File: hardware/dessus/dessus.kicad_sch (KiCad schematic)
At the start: 0 parts

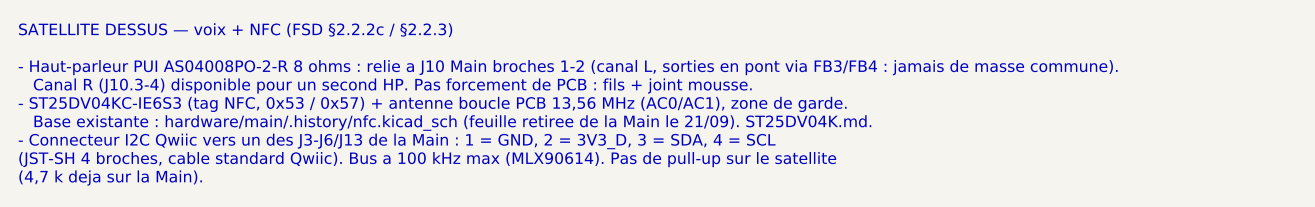
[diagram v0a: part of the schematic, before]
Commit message: hardware+docs: CAP1298 retenu pour le tactile de Cote 2, BOM de reference corrigee (H8)
- Cote 2 : CAP1298-1-SL-TR (C2652072, 8 touches, 0x28 fixe) remplace le MTCH2120
  (aucun stock) ; proximite de Cote 3 en suspens (pas de second CAP12xx).
- BOM : U11 = LSM6DSOXTR, doublon U21 retire, filtre DAC 470 ohm + 2,2 nF C0G,
  TMAG5273A1 (C3716049), U10 SOT-23-6, ecran bouche a choisir, LCSC de D1/Q1/Q2
  dans la bonne colonne, ST25DV et haut-parleur ajoutes.
- docs/pcb/02-bom-lcsc.csv (perimee) supprimee : une seule BOM.
- FSD, RESTE-A-FAIRE, syntheses et cartouches satellites alignes.
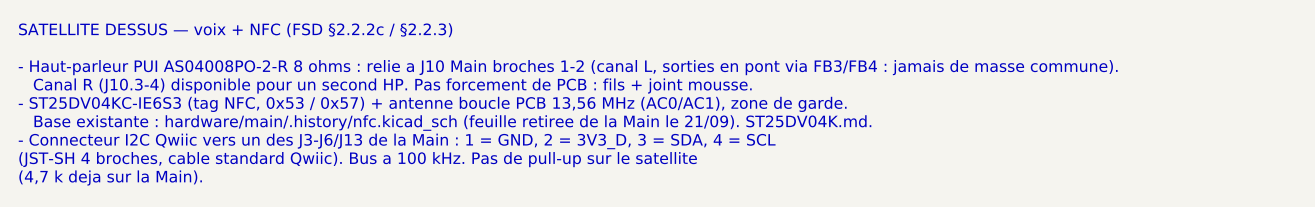
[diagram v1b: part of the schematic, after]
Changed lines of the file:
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@@
 	(generator_version "10.0")
 	(paper "A4")
-	(text "SATELLITE DESSUS — voix + NFC (FSD §2.2.2c / §2.2.3)\n\n- Haut-parleur PUI AS04008PO-2-R 8 ohms : relie a J10 Main broches 1-2 (canal L, sorties en pont via FB3/FB4 : jamais de masse commune).\n   Canal R (J10.3-4) disponible pour un second HP. Pas forcement de PCB : fils + joint mousse.\n- ST25DV04KC-IE6S3 (tag NFC, 0x53 / 0x57) + antenne boucle PCB 13,56 MHz (AC0/AC1), zone de garde.\n   Base existante : hardware/main/.history/nfc.kicad_sch (feuille retiree de la Main le 21/09). ST25DV04K.md.\n- Connecteur I2C Qwiic vers un des J3-J6/J13 de la Main : 1 = GND, 2 = 3V3_D, 3 = SDA, 4 = SCL\n(JST-SH 4 broches, cable standard Qwiic). Bus a 100 kHz max (MLX90614). Pas de pull-up sur le satellite\n(4,7 k deja sur la Main)."
+	(text "SATELLITE DESSUS — voix + NFC (FSD §2.2.2c / §2.2.3)\n\n- Haut-parleur PUI AS04008PO-2-R 8 ohms : relie a J10 Main broches 1-2 (canal L, sorties en pont via FB3/FB4 : jamais de masse commune).\n   Canal R (J10.3-4) disponible pour un second HP. Pas forcement de PCB : fils + joint mousse.\n- ST25DV04KC-IE6S3 (tag NFC, 0x53 / 0x57) + antenne boucle PCB 13,56 MHz (AC0/AC1), zone de garde.\n   Base existante : hardware/main/.history/nfc.kicad_sch (feuille retiree de la Main le 21/09). ST25DV04K.md.\n- Connecteur I2C Qwiic vers un des J3-J6/J13 de la Main : 1 = GND, 2 = 3V3_D, 3 = SDA, 4 = SCL\n(JST-SH 4 broches, cable standard Qwiic). Bus a 100 kHz. Pas de pull-up sur le satellite\n(4,7 k deja sur la Main)."
 		(exclude_from_sim no)
 		(at 20.32 142.24 0)

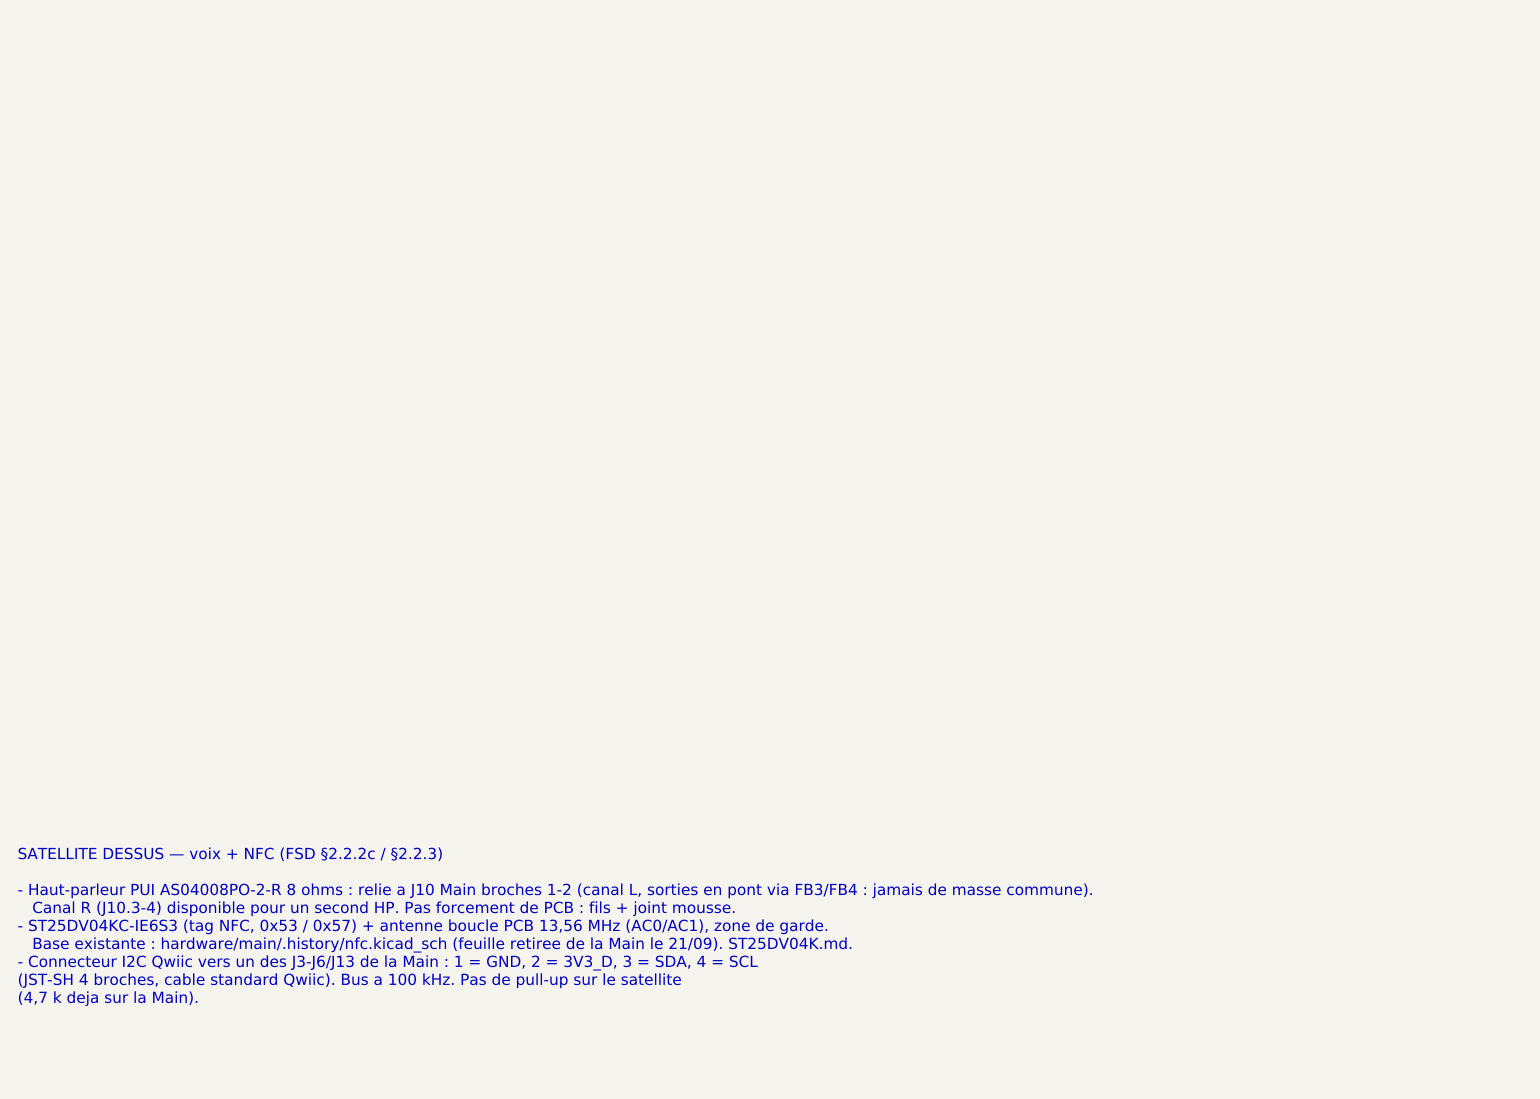
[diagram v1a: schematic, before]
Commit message: hardware: schemas des satellites Dessus, Devant, Cote 1 et Cote 3
- Dessus : ST25DV04KC (10 nF + 100 nF), antenne boucle ANT1 (~4,8 uH, empreinte a creer), accord C3 DNP, Qwiic
- Devant : BMP280 (CSB sur VDDIO, SDO GND), VEML7700, liaisons J7/J7b/J9, embases yeux/bouche provisoires, halo 8 WS2812B
- Cote 1 : ADS7830 ratiometrique, 4 faders PTA6043, 4 pots PDB181, liaison J8, toggles/boutons en facade sur JST-PH
- Cote 3 : TMAG5273A1 (INT et TEST a GND), 100 nF, Qwiic
- BOM : lignes satellites prefixees par face, recoupees avec les schemas
- Brochages corriges dans les syntheses : ST25DV (1 V_EH, 2 AC0) et VEML7700 (2 VDD, 4 SDA)
- Questions ouvertes : docs/audits/2026-09-27-questions-satellites.md
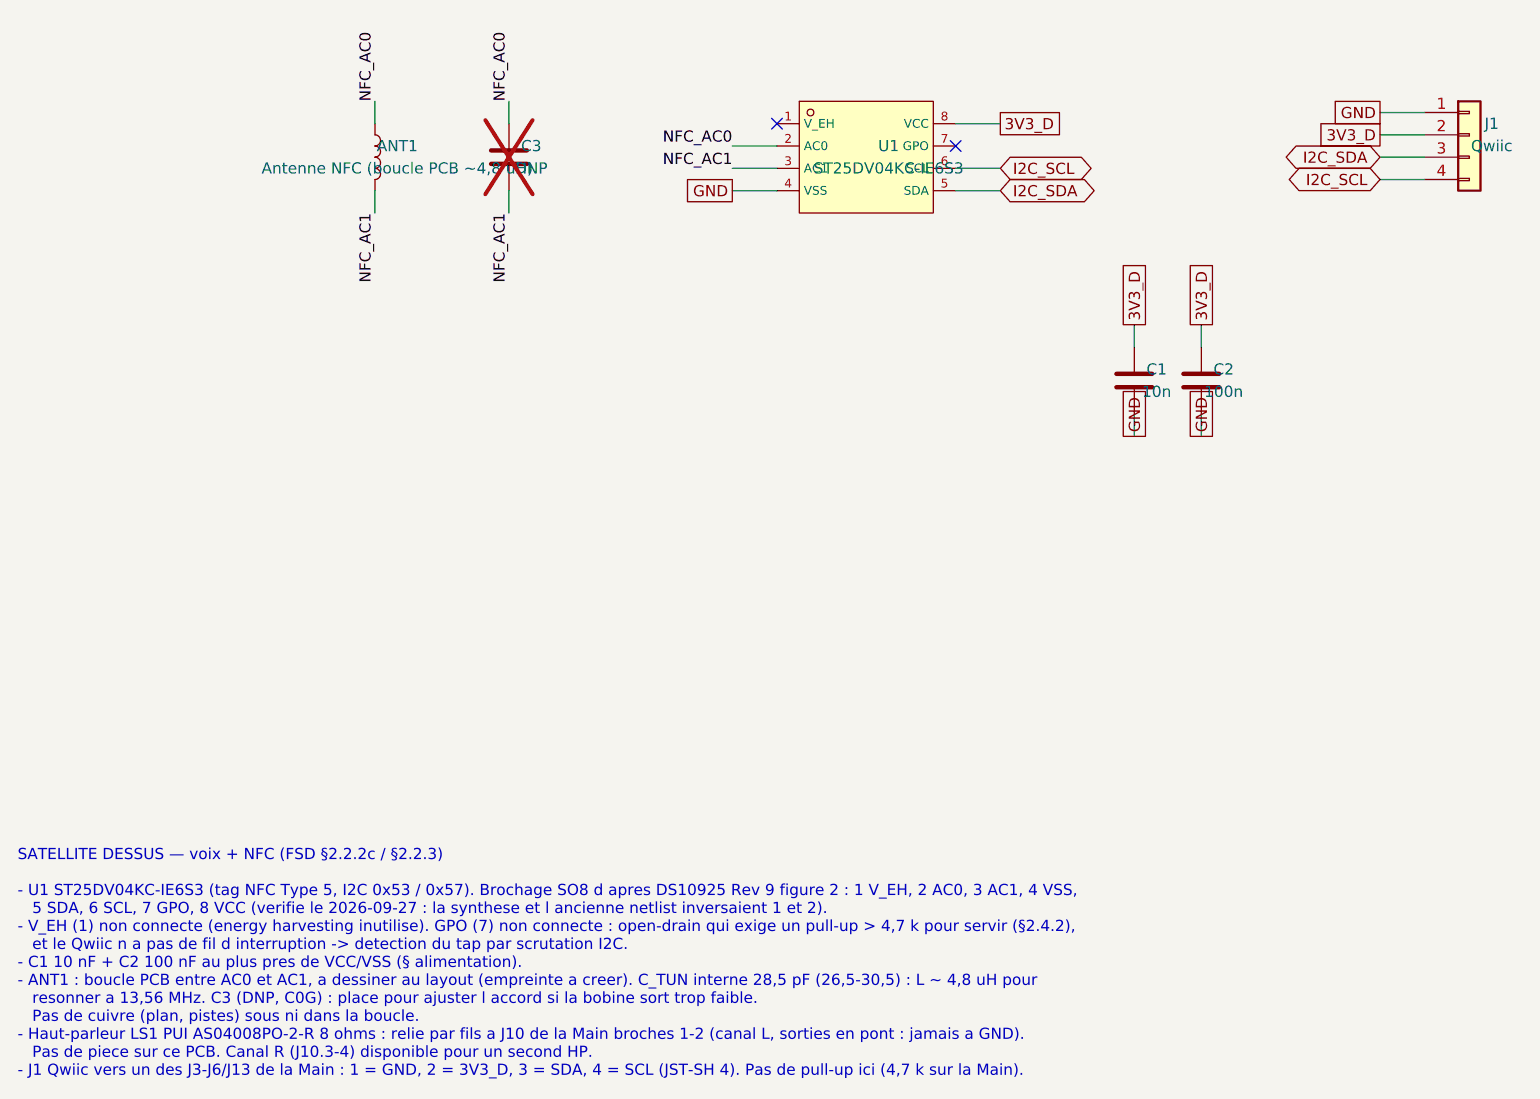
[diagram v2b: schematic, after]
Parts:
- added ANT1: Antenne NFC (boucle PCB ~4,8 uH), symbol Device:L
- added C1: 10n, Capacitor_SMD:C_0402_1005Metric, symbol Device:C
- added C2: 100n, Capacitor_SMD:C_0402_1005Metric, symbol Device:C
- added C3: DNP, Capacitor_SMD:C_0402_1005Metric, symbol Device:C
- added J1: Qwiic, Connector_JST:JST_SH_BM04B-SRSS-TB_1x04-1MP_P1.00mm_Vertical, symbol Connector_Generic:Conn_01x04
- added U1: ST25DV04KC-IE6S3, lcsc_footprints:C3304276_SO-8_L4_9-W3_9-P1_27-LS5_9-BL, symbol lcsc_imported:ST25DV04KC-IE6S3
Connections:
- new net 3V3_D: C1.1, C2.1, J1.2 (Pin_2), U1.8 (VCC)
- new net GND: C1.2, C2.2, J1.1 (Pin_1), U1.4 (VSS)
- new net I2C_SCL: J1.4 (Pin_4), U1.6 (SCL)
- new net I2C_SDA: J1.3 (Pin_3), U1.5 (SDA)
- new net NFC_AC0: ANT1.1, C3.1, U1.2 (AC0)
- new net NFC_AC1: ANT1.2, C3.2, U1.3 (AC1)
- no-connect marks 0 -> 2
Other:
- note added: "SATELLITE DESSUS — voix + NFC (FSD §2.2.2c / §2.2.3) - U1 ST25DV04KC-IE6S3 (tag NFC Type 5, I2C 0x53 / 0x57). Brochage SO8 d apres DS10925 Rev 9 figure 2 : 1 V_EH, 2 AC0, 3 AC1, 4 VSS, 5 SDA, 6 SCL, 7 GPO, 8 VCC (verifie le 2026-09-27 : la synthese et l ancienne netlist inversaient 1 et 2). - V_EH (1) non connecte (energy harvesting inutilise). GPO (7) non connecte : open-drain qui exige un pull-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"
- note removed: "SATELLITE DESSUS — voix + NFC (FSD §2.2.2c / §2.2.3) - Haut-parleur PUI AS04008PO-2-R 8 ohms : relie a J10 Main broches 1-2 (canal L, sorties en pont via FB3/FB4 : jamais de masse commune). Canal R (J10.3-4) disponible pour un second HP. Pas forcement de PCB : fils + joint mousse. - ST25DV04KC-IE6S3 (tag NFC, 0x53 / 0x57) + antenne boucle PCB 13,56 MHz (AC0/AC1), zone de garde. Base existante : h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"
